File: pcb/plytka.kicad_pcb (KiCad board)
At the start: 2 copper layers, 27 x 78 mm, 19 parts, among them J3 Battery, SW1 RESET, SW2 USER1, SW3 USER2, SW4 USER3

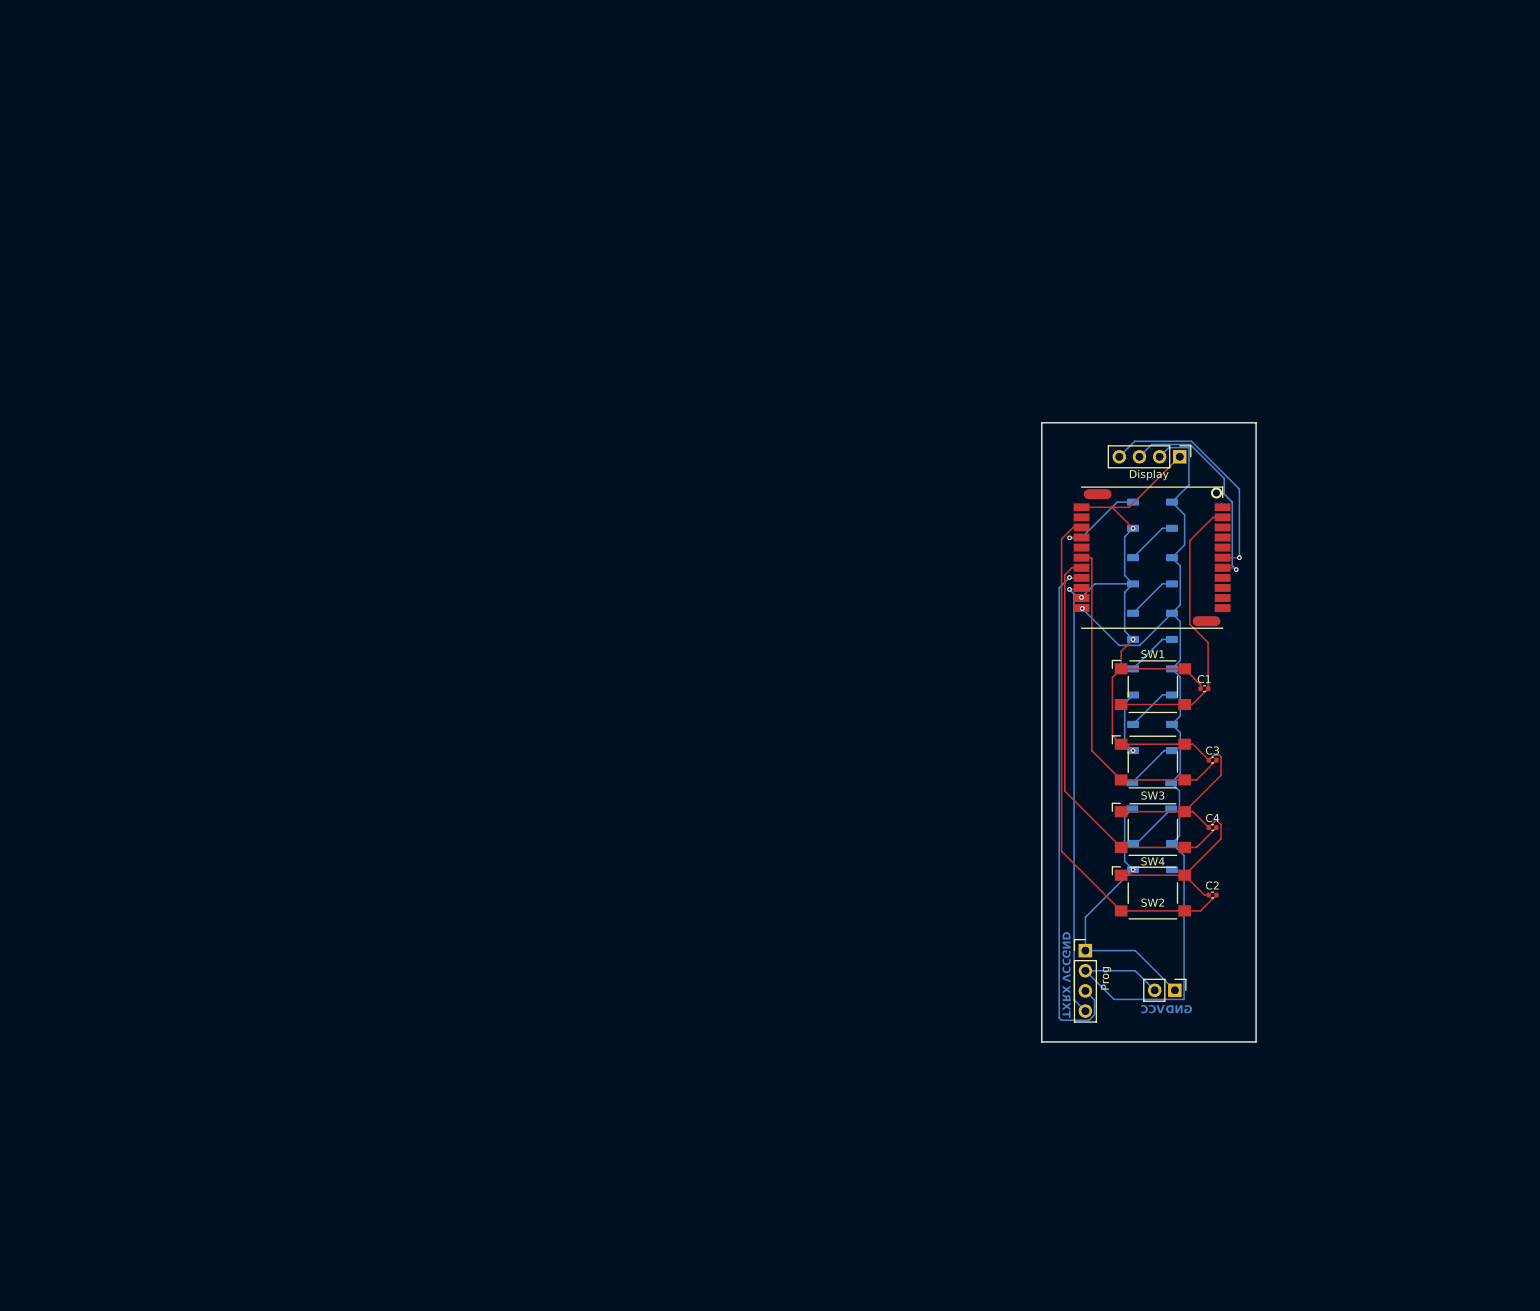
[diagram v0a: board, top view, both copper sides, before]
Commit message: pcb: add TPS61022 boost converter and simplify battery monitoring
- Add TPS61022 boost converter
- Simplify battery voltage sensing by removing DIVFET1 switched divider
- Update voltage divider values, now 1M and 1M + cap for stabilizing
- Add mode selection jumper for PFM/PWM switching
- Update battery capacity to ~500mAh
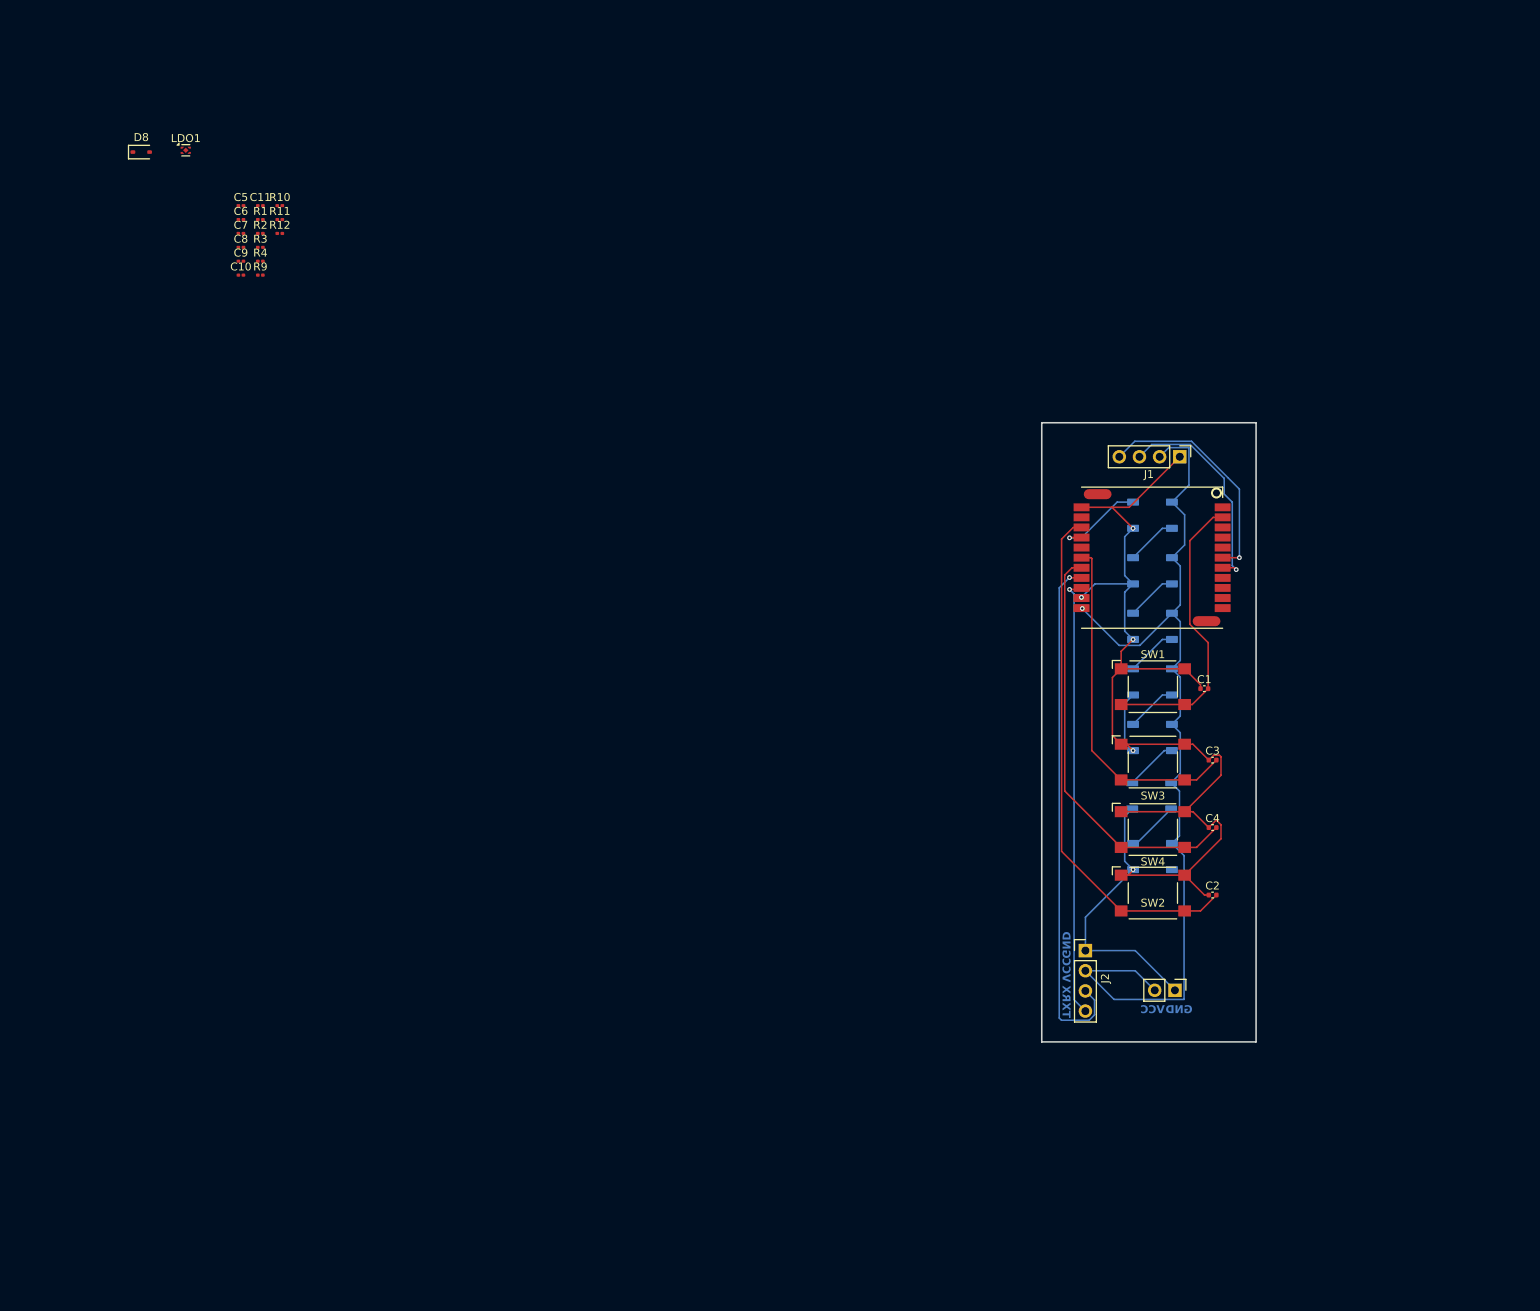
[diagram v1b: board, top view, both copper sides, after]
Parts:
- added C10: 100nF, Capacitor_SMD:C_0201_0603Metric, F.Cu at (28.6, 30.9)
- added C11: 100nF, Capacitor_SMD:C_0201_0603Metric, F.Cu at (31.1, 22.1)
- added C5: 4.7u, Capacitor_SMD:C_0201_0603Metric, F.Cu at (28.6, 22.1)
- added C6: 10u, Capacitor_SMD:C_0201_0603Metric, F.Cu at (28.6, 23.9)
- added C7: 10uF, Capacitor_SMD:C_0201_0603Metric, F.Cu at (28.6, 25.6)
- added C8: 100nF, Capacitor_SMD:C_0201_0603Metric, F.Cu at (28.6, 27.4)
- added C9: 10uF, Capacitor_SMD:C_0201_0603Metric, F.Cu at (28.6, 29.1)
- added D8: B5819WS SL, Diode_SMD:D_SOD-323, F.Cu at (16.1, 15.4)
- added LDO1: WL9005D4-33, Package_DFN_QFN:UDFN-4-1EP_1x1mm_P0.65mm_EP0.48x0.48mm, F.Cu at (21.7, 15.2)
- added R1: 20K, Resistor_SMD:R_0201_0603Metric, F.Cu at (31.1, 23.9)
- added R10: 1M, Resistor_SMD:R_0201_0603Metric, F.Cu at (33.5, 22.1)
- added R11: 100K, Resistor_SMD:R_0201_0603Metric, F.Cu at (33.5, 23.9)
- added R12: 100R, Resistor_SMD:R_0201_0603Metric, F.Cu at (33.5, 25.6)
- added R2: 1K, Resistor_SMD:R_0201_0603Metric, F.Cu at (31.1, 25.6)
- added R3: 5.1K, Resistor_SMD:R_0201_0603Metric, F.Cu at (31.1, 27.4)
- added R4: 5.1K, Resistor_SMD:R_0201_0603Metric, F.Cu at (31.1, 29.1)
- added R9: 470K, Resistor_SMD:R_0201_0603Metric, F.Cu at (31.1, 30.9)
- renumbered Display to J1, Prog to J2
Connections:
- HTCC-AM1 pad 1: VCC -> 3V3
- J1 pad 2: VCC -> 3V3
- J2 pad 2: VCC -> unconnected-(J2-Pin_2-Pad2)
- J3 pad 2: VCC -> BAT+

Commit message: aktualna wersja
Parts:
- added C11: 100n, Capacitor_SMD:C_0201_0603Metric, F.Cu at (62.7, 39.0)
- added C16: 10 uF, Capacitor_SMD:C_0805_2012Metric, F.Cu at (47.0, 39.1)
- added C17: 100n, Capacitor_SMD:C_0402_1005Metric, F.Cu at (61.9, 26.6)
- added C18: 100n, Capacitor_SMD:C_0402_1005Metric, F.Cu at (61.9, 28.6)
- added D9: D_Schottky, Diode_SMD:D_SMA, F.Cu at (60.5, 23.3)
- added J4: USB_C_Receptacle_USB2.0_16P, Connector_USB:USB_C_Receptacle_G-Switch_GT-USB-7010ASV, F.Cu at (50.6, 26.4)
- added Q1: SS8050, Package_TO_SOT_SMD:SOT-23, F.Cu at (56.1, 33.4)
- added Q2: SS8050, Package_TO_SOT_SMD:SOT-23, F.Cu at (56.1, 37.8)
- added R11: 10k, Resistor_SMD:R_01005_0402Metric, F.Cu at (50.3, 38.4)
- added R12: 10k, Resistor_SMD:R_0402_1005Metric, F.Cu at (60.0, 39.1)
- added R2: 5.1 k, Resistor_SMD:R_0603_1608Metric, F.Cu at (58.4, 26.9)
- added R3: 5.1k, Resistor_SMD:R_0603_1608Metric, F.Cu at (58.4, 29.4)
- added U1: TPS61022, Package_DFN_QFN:Texas_RWU0007A_VQFN-7_2x2mm_P0.5mm, F.Cu at (60.8, 32.9)
- added U3: USBLC6-2P6, Package_TO_SOT_SMD:SOT-666, F.Cu at (60.5, 36.5)
- added U4: CH340K, Package_SO:SSOP-10-1EP_3.9x4.9mm_P1mm_EP2.1x3.3mm, F.Cu at (49.4, 34.4)
- C1, C2, C3, C4: value 100uF -> 100n
- C10, C8: value 100nF -> 100n
- C7, C9: value 10uF -> 10u
- R1: value 20K -> 2.5K
- R9: value 470K -> 1M
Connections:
- net VCC renamed LED5V
- D1 pad 4: GPIO2 -> Net-(D1-DIN)
- HTCC-AM1 pad 18: unconnected-(HTCC-AM1-GPIO0-Pad18) -> GPIO1
- HTCC-AM1 pad 19: unconnected-(HTCC-AM1-GPIO5-Pad19) -> CHGSTAT
- HTCC-AM1 pad 9: GPIO1 -> BOOST_EN
- J2 pad 2: unconnected-(J2-Pin_2-Pad2) -> 3V3
- J3 pad 2: BAT+ -> VBAT
- R9 pad 1: Net-(DIVFET1-S) -> VBAT
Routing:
- net LED5V: track 119.6 -> 0.00 mm
- net (no net): track 0.00 -> 119.6 mm

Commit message: update
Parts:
- removed the C11 at (62.7, 39.0)
- removed the C11 at (31.1, 22.1)
- removed D9: D_Schottky, Diode_SMD:D_SMA
- removed J3: Battery, Connector_PinHeader_2.54mm:PinHeader_1x02_P2.54mm_Vertical
- removed J4: USB_C_Receptacle_USB2.0_16P, Connector_USB:USB_C_Receptacle_G-Switch_GT-USB-7010ASV
- removed Q1, Q2: SS8050, Package_TO_SOT_SMD:SOT-23
- removed R11: 100K, Resistor_SMD:R_0201_0603Metric
- removed R11: 10k, Resistor_SMD:R_01005_0402Metric
- removed R12: 100R, Resistor_SMD:R_0201_0603Metric
- removed R12: 10k, Resistor_SMD:R_0402_1005Metric
- removed the R2 at (31.1, 25.6)
- removed the R2 at (58.4, 26.9)
- removed the R3 at (31.1, 27.4)
- removed the R3 at (58.4, 29.4)
- removed R4: 5.1K, Resistor_SMD:R_0201_0603Metric
- added BT1: 3.7V ~500mAh, Connector_PinHeader_2.54mm:PinHeader_1x02_P2.54mm_Vertical, F.Cu at (12.4, 15.2)
- added C11: 100n, Capacitor_SMD:C_0201_0603Metric, F.Cu at (8.82, 10.3)
- added C12: 10u, Capacitor_SMD:C_0201_0603Metric, F.Cu at (8.82, 12.1)
- added C13: 22u, Capacitor_SMD:C_1206_3216Metric, F.Cu at (2.33, 1.18)
- added C14: 22u, Capacitor_SMD:C_1206_3216Metric, F.Cu at (2.33, 4.53)
- added C15: 22u, Capacitor_SMD:C_1206_3216Metric, F.Cu at (2.33, 7.88)
- added JP1: Jumper_3_Bridged12, Jumper:SolderJumper-3_P1.3mm_Bridged2Bar12_Pad1.0x1.5mm, F.Cu at (17.5, 19.3)
- added L1: 1uH (2-3A saturation), Inductor_SMD:L_1008_2520Metric, F.Cu at (15.0, 7.83)
- added Q3: AO3400A, Package_TO_SOT_SMD:SOT-23, F.Cu at (7.61, 15.2)
- added Q4: AO3400A, Package_TO_SOT_SMD:SOT-23, F.Cu at (7.61, 19.6)
- added R2: 5.1 k, Resistor_SMD:R_0603_1608Metric, F.Cu at (1.50, 10.8)
- added R3: 5.1k, Resistor_SMD:R_0603_1608Metric, F.Cu at (1.50, 13.3)
- added R5: 470R, Resistor_SMD:R_0402_1005Metric, F.Cu at (18.9, 10.4)
- added R6: 732k, Resistor_SMD:R_0603_1608Metric, F.Cu at (1.50, 15.8)
- added R7: 100k, Resistor_SMD:R_0603_1608Metric, F.Cu at (1.50, 18.3)
- added U2: TP4054, Library:SOT-23-5, F.Cu at (17.2, 15.3)
- C16: value 10 uF -> 100n; footprint Capacitor_SMD:C_0805_2012Metric -> Capacitor_SMD:C_0402_1005Metric
- C5: value 4.7u -> 10u
- SW2: value USER1 -> USER0
- moved C17 52.3 mm to (15.5, 2.46)
- moved C18 52.3 mm to (15.5, 4.42)
- moved U1 52.3 mm to (19.1, 1.27)
- moved U4 50.7 mm to (9.78, 2.73)
- moved U3 50.1 mm to (19.5, 7.78)
- moved C16 49.8 mm to (15.5, 0.48)
- moved C10 29.8 mm to (8.82, 8.57)
- moved C9 29.8 mm to (8.82, 6.83)
- moved R9 29.8 mm to (11.3, 8.57)
- moved C5 27.0 mm to (6.38, 6.83)
- moved C6 27.0 mm to (6.38, 8.57)
- moved C7 27.0 mm to (6.38, 10.3)
- moved C8 27.0 mm to (6.38, 12.1)
- moved R1 26.1 mm to (11.3, 6.83)
- moved R10 25.2 mm to (11.3, 10.3)
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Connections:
- net GPIO1 renamed GPIO0
- C16 pad 1: 5V -> DTR
- C16 pad 2: GND -> RESET
- U3 pad 1: D- -> Net-(J3-D--PadA7)
- U3 pad 3: D+ -> Net-(J3-D+-PadA6)
- U3 pad 4: Net-(J4-CC2) -> D+
- U3 pad 5: Net-(D9-K) -> 5V
- U3 pad 6: Net-(J4-CC1) -> D-
- U4 pad 8: UART_TX -> UART_RX
- U4 pad 9: UART_RX -> UART_TX
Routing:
- net GND: track 171.3 -> 0.00 mm, vias 5 -> 0
- net (no net): track 119.6 -> 0.00 mm
- net UART_RX: track 66.0 -> 0.00 mm, vias 1 -> 0
- net GPIO0: track 65.9 -> 0.00 mm
- net UART_TX: track 55.5 -> 0.00 mm, vias 1 -> 0
- net GPIO7: track 52.8 -> 0.00 mm
- net GPIO6: track 43.8 -> 0.00 mm
- net RESET: track 36.7 -> 0.00 mm
- net SDA: track 29.2 -> 0.00 mm, vias 1 -> 0
- net SCL: track 27.1 -> 0.00 mm, vias 1 -> 0
- net GPIO2: track 11.4 -> 0.00 mm, vias 1 -> 0
- net Net-(D5-DOUT): track 6.68 -> 0.00 mm
- net Net-(D6-DOUT): track 6.60 -> 0.00 mm
- net Net-(D4-DOUT): track 6.43 -> 0.00 mm
- net Net-(D3-DOUT): track 6.43 -> 0.00 mm
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
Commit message: lcsc
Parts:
- added J3: USB_C_Receptacle_USB2.0_16P, Connector_USB:USB_C_Receptacle_G-Switch_GT-USB-7010ASV, F.Cu at (85.9, 155.6)
- SW1, SW2, SW3, SW4: footprint Button_Switch_SMD:SW_SPST_Omron_B3FS-100xP -> Button_Switch_THT:SW_TH_Tactile_Omron_B3F-100x
- moved R2 158.4 mm to (79.7, 148.6)
- moved U4 158.1 mm to (85.4, 141.6)
- moved U3 154.9 mm to (84.1, 148.6)
- moved R3 154.1 mm to (79.7, 146.1)
- moved C17 152.5 mm to (79.0, 141.1)
- moved C18 149.5 mm to (76.0, 141.1)
- moved C5 136.7 mm to (85.2, 118.5)
- moved R1 131.9 mm to (85.2, 116.0)
- moved C6 131.3 mm to (85.2, 113.5)
- moved D8 131.0 mm to (89.7, 118.5)
- moved BT1 128.8 mm to (94.2, 114.7)
- moved U2 122.7 mm to (89.4, 114.5)
- moved R5 121.5 mm to (132.5, 53.5)
- moved C11 120.0 mm to (111.5, 72.5)
- moved C10 119.6 mm to (103.7, 81.5)
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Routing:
- net GND: track 0.00 -> 8.40 mm
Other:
- board size 27 x 78 mm -> 33.5 x 88 mm

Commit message: almost finish pcb
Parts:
- removed J2: Program, Connector_PinHeader_2.54mm:PinHeader_1x04_P2.54mm_Vertical
- added G*** (x2): LOGO, LOGO, F.Cu at (154.8, 114.5)
- added G***: LOGO, LOGO, F.Cu at (154.1, 100.9)
- added REF**: MountingHole_2.1mm, MountingHole:MountingHole_2.1mm, F.Cu at (154.6, 54.6)
- added REF**: MountingHole_2.1mm, MountingHole:MountingHole_2.1mm, F.Cu at (154.5, 126.4)
- added REF**: MountingHole_2.1mm, MountingHole:MountingHole_2.1mm, F.Cu at (131.4, 54.6)
- C10, C11, C8: footprint Capacitor_SMD:C_0201_0603Metric -> Capacitor_SMD:C_0402_1005Metric
- C12, C5, C6, C7, C9: footprint Capacitor_SMD:C_0201_0603Metric -> Capacitor_SMD:C_0603_1608Metric
- C13, C14, C15: footprint Capacitor_SMD:C_1206_3216Metric -> Capacitor_SMD:C_0603_1608Metric
- D1, D2, D3, D4, D5, D6, D7: moved to F.Cu
- HTCC-AM1: moved to B.Cu
- SW1: renamed from SW2; footprint Button_Switch_THT:SW_TH_Tactile_Omron_B3F-100x -> Button_Switch_SMD:SW_Push_1P1T-MP_NO_Horizontal_Alps_SKRTLAE010
- SW2: renamed from SW3; value USER2 -> USER6; footprint Button_Switch_THT:SW_TH_Tactile_Omron_B3F-100x -> Button_Switch_SMD:SW_Push_1P1T-MP_NO_Horizontal_Alps_SKRTLAE010
- SW3: renamed from SW4; value USER3 -> USER7; footprint Button_Switch_THT:SW_TH_Tactile_Omron_B3F-100x -> Button_Switch_SMD:SW_Push_1P1T-MP_NO_Horizontal_Alps_SKRTLAE010
- SW4: renamed from SW1; footprint Button_Switch_THT:SW_TH_Tactile_Omron_B3F-100x -> Button_Switch_SMD:SW_Push_1P1T-MP_NO_Horizontal_Alps_SKRTLAE010
- moved R6 94.3 mm to (138.2, 106.9), turned to 180 degrees
- moved U1 91.9 mm to (136.9, 109.2), turned to 180 degrees
- moved C13 91.3 mm to (140.6, 109.3), turned to -90 degrees
- moved C14 88.2 mm to (143.0, 109.3), turned to -90 degrees
- moved R7 87.3 mm to (135.2, 106.9), turned to 180 degrees
- moved C15 85.8 mm to (145.4, 109.3), turned to -90 degrees
- moved C12 85.2 mm to (134.4, 109.2), turned to 90 degrees
- moved L1 79.9 mm to (134.8, 112.2)
- moved JP1 71.6 mm to (132.3, 108.2), turned to -90 degrees
- moved R3 70.6 mm to (145.7, 121.1), turned to 180 degrees
- moved R2 66.8 mm to (140.7, 121.3)
- moved C18 66.6 mm to (138.0, 116.6), turned to -90 degrees
- moved Q4 64.6 mm to (136.5, 58.0), turned to 180 degrees
- moved J3 63.9 mm to (143.0, 126.9)
- moved C16 63.8 mm to (134.6, 60.3), turned to 180 degrees
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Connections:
- HTCC-AM1 pad 10: unconnected-(HTCC-AM1-ADC-Pad10) -> BAT_LVL
- U3 pad 1: Net-(J3-D--PadA7) -> Net-(J3-D+-PadA6)
- U3 pad 3: Net-(J3-D+-PadA6) -> Net-(J3-D--PadA7)
- U3 pad 4: D+ -> D-
- U3 pad 6: D- -> D+
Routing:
- net GND: track 8.40 -> 110.2 mm, vias 0 -> 22
- net 3V3: track 0.00 -> 95.0 mm, vias 0 -> 1
- net DTR: track 0.00 -> 68.5 mm, vias 0 -> 2
- net RTS: track 0.00 -> 62.5 mm, vias 0 -> 2
- net UART_TX: track 0.00 -> 61.4 mm, vias 0 -> 1
- net UART_RX: track 0.00 -> 61.1 mm, vias 0 -> 1
- net BOOST_EN: track 0.00 -> 60.9 mm, vias 0 -> 3
- net BAT_LVL: track 0.00 -> 56.2 mm, vias 0 -> 6
- net RESET: track 0.00 -> 52.5 mm, vias 0 -> 5
- net Net-(D1-DIN): track 0.00 -> 49.2 mm, vias 0 -> 2
- net VBAT: track 0.00 -> 43.8 mm, vias 0 -> 2
- net GPIO0: track 0.00 -> 37.5 mm, vias 0 -> 5
- net CHGSTAT: track 0.00 -> 36.8 mm, vias 0 -> 1
- net Net-(D8-K): track 0.00 -> 24.1 mm, vias 0 -> 2
- net GPIO7: track 0.00 -> 23.1 mm, vias 0 -> 3
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- added copper zone on B.Cu, net GND
- added copper zone on F.Cu, net GND
- added copper zone on F.Cu, net LED5V
- added copper zone on F.Cu, net Net-(U1-SW)
- added copper zone on F.Cu, net VBAT
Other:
- board size 33.5 x 88 mm -> 29.2 x 77.9 mm
- board text added: "v1.0"
- board text added: "Łowy na lisa"
- board text removed: "GND"
- board text removed: "RX"
- board text removed: "TX"
- board text removed: "VCC"

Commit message: lcsc
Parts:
- added R4: 220k, Resistor_SMD:R_0603_1608Metric, F.Cu at (136.7, 105.4)
- R1: value 2.5K -> 2.4k; footprint Resistor_SMD:R_0201_0603Metric -> Resistor_SMD:R_0603_1608Metric
- R10, R9: footprint Resistor_SMD:R_0201_0603Metric -> Resistor_SMD:R_0402_1005Metric
- R2: value 5.1 k -> 5.1k
- R6: value 732k -> 510k
- moved R1 3.00 mm to (138.2, 95.5), turned to -90 degrees
- moved R9 0.90 mm to (133.9, 102.6)
- moved R10 0.73 mm to (134.9, 101.6)
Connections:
- R6 pad 2: Net-(U1-FB) -> Net-(R4-Pad1)
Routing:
- net Net-(R4-Pad1): track 0.00 -> 1.56 mm
- net BAT_LVL: track 56.2 -> 57.5 mm
- net VBAT: track 43.8 -> 44.8 mm
